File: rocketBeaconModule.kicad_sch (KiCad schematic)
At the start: 42 parts, among them J1 TYPE-C-31-M-12, J2 PWR, J3 GND, J4 PWR, J5 GND, U1 STM32F401CCU6, U2 CP2102N-Axx-xQFN20, Y1 16MHz

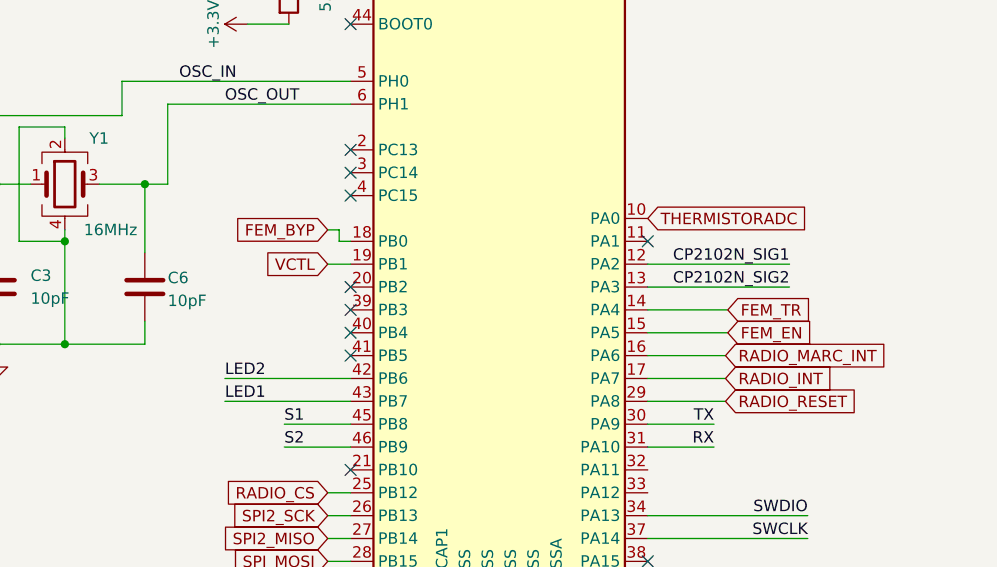
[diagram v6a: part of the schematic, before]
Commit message: fixed temp sensor and updated digpot stm32 connections
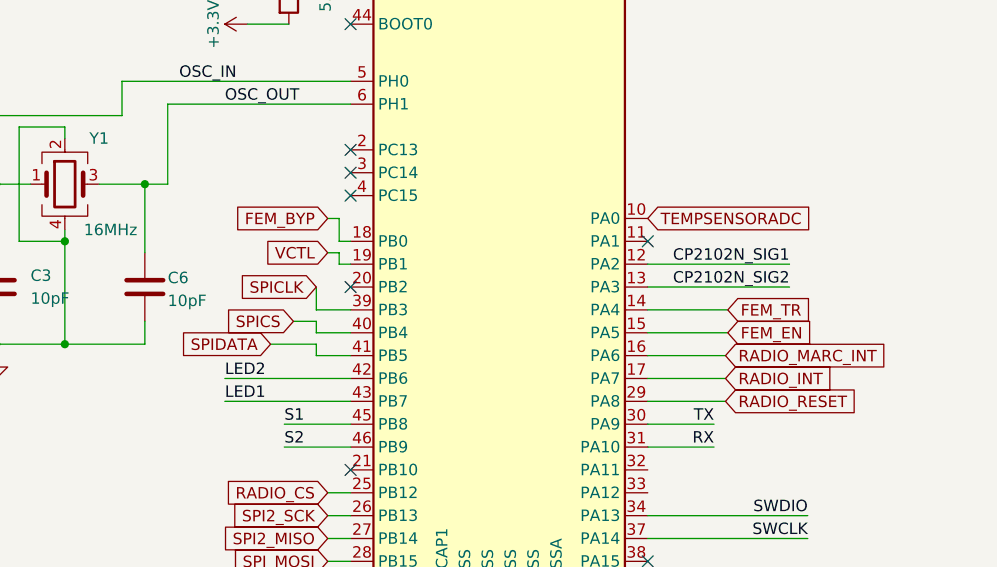
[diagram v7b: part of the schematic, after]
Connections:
- net SPICLK: now reaches U1.39 (PB3)
- net SPICS: now reaches U1.40 (PB4)
- net SPIDATA: now reaches U1.41 (PB5)
- net THERMISTORADC renamed TEMPSENSORADC
- no-connect marks 19 -> 16
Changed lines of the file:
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@@
-	)
-	(no_connect
-		(at 118.11 88.9)
 	)
 	(no_connect
@@
 	)
 	(no_connect
-		(at 118.11 91.44)
-	)
-	(no_connect
 		(at 240.03 114.808)
 	)
@@
 	)
 	(no_connect
-		(at 118.11 86.36)
-	)
-	(no_connect
 		(at 240.03 132.588)
 	)
@@
 	(wire
 		(pts
-			(xy 115.57 81.28) (xy 118.11 81.28)
+			(xy 115.57 80.01) (xy 116.84 80.01)
 		)
 		(stroke
@@
 	(wire
 		(pts
+			(xy 114.3 91.44) (xy 114.3 90.17)
+		)
+		(stroke
+			(width 0)
+			(type default)
+		)
+	)
+	(wire
+		(pts
 			(xy 160.02 86.36) (xy 151.13 86.36)
 		)
@@
 	(wire
 		(pts
+			(xy 114.3 88.9) (xy 118.11 88.9)
+		)
+		(stroke
+			(width 0)
+			(type default)
+		)
+	)
+	(wire
+		(pts
 			(xy 86.36 78.74) (xy 86.36 90.17)
 		)
@@
 		)
 	)
+	(wire
+		(pts
+			(xy 111.76 87.63) (xy 114.3 87.63)
+		)
+		(stroke
+			(width 0)
+			(type default)
+		)
+	)
 	(polyline
 		(pts
@@
 	(wire
 		(pts
-			(xy 115.57 77.47) (xy 116.84 77.47)
+			(xy 116.84 80.01) (xy 116.84 81.28)
+		)
+		(stroke
+			(width 0)
+			(type default)
+		)
+	)
+	(wire
+		(pts
+			(xy 115.57 76.2) (xy 116.84 76.2)
 		)
 		(stroke
@@
 	(wire
 		(pts
+			(xy 114.3 86.36) (xy 118.11 86.36)
+		)
+		(stroke
+			(width 0)
+			(type default)
+		)
+	)
+	(wire
+		(pts
 			(xy 13.462 161.29) (xy 24.13 161.29)
 		)
@@
 	(wire
 		(pts
+			(xy 116.84 81.28) (xy 118.11 81.28)
+		)
+		(stroke
+			(width 0)
+			(type default)
+		)
+	)
+	(wire
+		(pts
 			(xy 63.5 34.29) (xy 63.5 35.56)
 		)
@@
 	(wire
 		(pts
+			(xy 114.3 83.82) (xy 114.3 86.36)
+		)
+		(stroke
+			(width 0)
+			(type default)
+		)
+	)
+	(wire
+		(pts
 			(xy 153.67 30.48) (xy 153.67 33.02)
 		)
@@
 	(wire
 		(pts
+			(xy 109.22 90.17) (xy 114.3 90.17)
+		)
+		(stroke
+			(width 0)
+			(type default)
+		)
+	)
+	(wire
+		(pts
 			(xy 151.13 109.22) (xy 168.91 109.22)
 		)
@@
 	(wire
 		(pts
+			(xy 118.11 91.44) (xy 114.3 91.44)
+		)
+		(stroke
+			(width 0)
+			(type default)
+		)
+	)
+	(wire
+		(pts
+			(xy 114.3 87.63) (xy 114.3 88.9)
+		)
+		(stroke
+			(width 0)
+			(type default)
+		)
+	)
+	(wire
+		(pts
 			(xy 268.986 56.642) (xy 267.208 56.642)
 		)
@@
 	(wire
 		(pts
-			(xy 116.84 77.47) (xy 116.84 78.74)
+			(xy 116.84 76.2) (xy 116.84 78.74)
 		)
 		(stroke
@@
 	(global_label "VCTL"
 		(shape input)
-		(at 115.57 81.28 180)
+		(at 115.57 80.01 180)
 		(fields_autoplaced yes)
 		(effects
@@
 		)
 		(property "Intersheetrefs" "${INTERSHEET_REFS}"
-			(at 108.2305 81.28 0)
+			(at 108.2305 80.01 0)
 			(effects
 				(font
@@
 	(global_label "FEM_BYP"
 		(shape input)
-		(at 115.57 77.47 180)
+		(at 115.57 76.2 180)
 		(fields_autoplaced yes)
 		(effects
@@
 		)
 		(property "Intersheetrefs" "${INTERSHEET_REFS}"
-			(at 104.2996 77.47 0)
+			(at 104.2996 76.2 0)
 			(effects
 				(font
@@
 		)
 	)
+	(global_label "SPIDATA"
+		(shape input)
+		(at 109.22 90.17 180)
+		(fields_autoplaced yes)
+		(effects
+			(font
+				(size 1.27 1.27)
+			)
+			(justify right)
+		)
+		(property "Intersheetrefs" "${INTERSHEET_REFS}"
+			(at 98.7357 90.17 0)
+			(effects
+				(font
+					(size 1.27 1.27)
+				)
+				(justify right)
+				(hide yes)
+			)
+		)
+	)
+	(global_label "SPICS"
+		(shape input)
+		(at 111.76 87.63 180)
+		(fields_autoplaced yes)
+		(effects
+			(font
+				(size 1.27 1.27)
+			)
+			(justify right)
+		)
+		(property "Intersheetrefs" "${INTERSHEET_REFS}"
+			(at 103.211 87.63 0)
+			(effects
+				(font
+					(size 1.27 1.27)
+				)
+				(justify right)
+				(hide yes)
+			)
+		)
+	)
 	(global_label "RADIO_RESET"
 		(shape input)
@@
 		)
 	)
-	(global_label "THERMISTORADC"
+	(global_label "SPICLK"
+		(shape input)
+		(at 114.3 83.82 180)
+		(fields_autoplaced yes)
+		(effects
+			(font
+				(size 1.27 1.27)
+			)
+			(justify right)
+		)
+		(property "Intersheetrefs" "${INTERSHEET_REFS}"
+			(at 104.6624 83.82 0)
+			(effects
+				(font
+					(size 1.27 1.27)
+				)
+				(justify right)
+				(hide yes)
+			)
+		)
+	)
+	(global_label "TEMPSENSORADC"
 		(shape input)
 		(at 151.13 76.2 0)
@@
 		)
 		(property "Intersheetrefs" "${INTERSHEET_REFS}"
-			(at 169.2947 76.2 0)
+			(at 170.0808 76.2 0)
 			(effects
 				(font
